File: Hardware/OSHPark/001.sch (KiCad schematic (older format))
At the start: 23 parts, among them J1 CONN_01X02, J2 CONN_01X03, J3 CONN_01X03, J4 CONN_02X03, J5 CONN_01X02, U1 LM340MP-5.0/NOPB, U2 ATTINY85-20SU

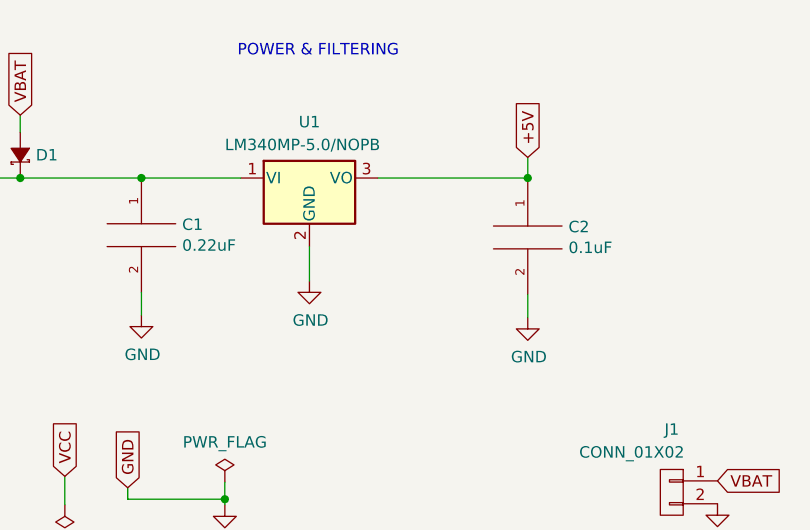
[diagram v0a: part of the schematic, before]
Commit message: Update Capacitors Value en Voltage Regulator
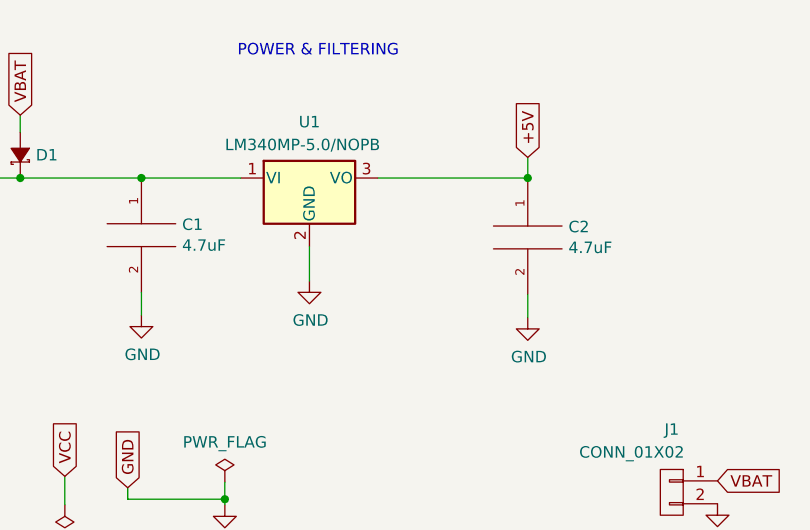
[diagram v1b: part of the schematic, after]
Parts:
- C1: value 0.22uF -> 4.7uF
- C2: value 0.1uF -> 4.7uF
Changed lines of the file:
@@
 P 7305 1425
 F 0 "C1" H 7483 1471 50  0000 L CNN
-F 1 "0.22uF" H 7483 1380 50  0000 L CNN
+F 1 "4.7uF" H 7483 1380 50  0000 L CNN
 F 2 "Capacitors_SMD:C_1206_HandSoldering" H 7305 1425 50  0001 C CNN
 F 3 "" H 7305 1425 50  0001 C CNN
@@
 P 8995 1435
 F 0 "C2" H 9173 1481 50  0000 L CNN
-F 1 "0.1uF" H 9173 1390 50  0000 L CNN
+F 1 "4.7uF" H 9173 1390 50  0000 L CNN
 F 2 "Capacitors_SMD:C_1206_HandSoldering" H 8995 1435 50  0001 C CNN
 F 3 "" H 8995 1435 50  0001 C CNN
